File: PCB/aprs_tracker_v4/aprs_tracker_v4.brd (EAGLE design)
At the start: 100 x 35 mm, 43 parts, among them IC1 7805T, IC2 ATMEGA328PB-AUR, IC3 74LVCH1T45GW,125, IC4 REG1117, T1 2N2222, X1 BU-SMA-V, Y1 ATS080B-E

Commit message: completed aprs v4
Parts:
- removed C3: 4.7u, rcl:C050-024X044
- removed JP2: (no value), pinhead:2X03/90
- removed LED1, LED2, LED3, LED4, LED5: (no value), led:CHIP-LED0805
- added D1, D2, D3, D4, D5: (no value), led:CHIP-LED0805
- added JP4: (no value), pinhead:2X03/90
- added JP5: (no value), pinhead:2X04
- C4: device rcl:C1206 -> rcl:C0805
- C5, C7, C8, C9: device rcl:E5-6 -> rcl:C0805
- C6: device rcl:C050-024X044 -> rcl:C0805
- JP1: device pinhead:2X02 -> pinhead:2X03/90
- R1, R10, R11, R3, R5, R7, R8: device rcl:0207/7 -> rcl:R0805
- R4: device rcl:0204/7 -> rcl:R0805
- moved C9 151.0 mm to (54.2, 22.4)
- moved C8 142.3 mm to (49.2, 22.4), turned to 180 degrees
- moved R15 131.5 mm to (65.3, 7.75), turned to 180 degrees
- moved IC4 131.4 mm to (52.6, 16.0), turned to 180 degrees
- moved R6 120.4 mm to (18.8, 32.3), turned to 270 degrees
- moved S1 110.9 mm to (24.9, 30.5)
- moved C5 109.7 mm to (96.3, 9.21), turned to 90 degrees
- moved C7 103.6 mm to (96.3, 15.4), turned to 90 degrees
- moved C2 98.5 mm to (20.1, 22.9), turned to 90 degrees
- moved IC3 94.7 mm to (66.0, 10.4), turned to 90 degrees
- moved C1 87.2 mm to (20.1, 15.2), turned to 90 degrees
- moved IC1 84.0 mm to (81.7, 13.0), turned to 90 degrees
- moved Y1 79.5 mm to (15.2, 16.0), turned to 90 degrees
- moved R2 55.6 mm to (30.4, 3.30), turned to 180 degrees
- moved IC2 53.3 mm to (27.7, 18.8), flipped to the bottom
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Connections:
- new net A63: D2.A, U1.P$5
- net +3V3: now also C9.1; no longer C9.+
- net A6: no longer LED2.A, U1.P$5
- net GND: now also C5.2, C7.2, C8.2, C9.2, JP1.5, JP4.5, JP4.6, JP5.1; no longer C5.-, C7.-, C8.-, C9.-, JP1.1, JP1.3, JP2.1
- net N$10: no longer C3.2
- net N$11: no longer C3.1, R9.1
- net N$20: now also D3.C; no longer LED1.C
- net N$21: now also D2.C; no longer LED2.C
- net N$22: now also D4.C; no longer LED3.C
- net N$23: now also D3.A; no longer LED1.A
- net N$3: now also D1.C; no longer LED4.C
- net N$5: now also D5.C; no longer LED5.C
- net PIN11: now also JP4.3, JP5.3; no longer JP1.4, JP2.3
- net PIN12: now also JP4.4, JP5.6; no longer JP1.2, JP2.6
- net PIN9: now also JP1.4
- net RADIO_SQL: now also D4.A; no longer LED3.A
- net RESET: now also JP5.2; no longer JP2.2
- net RX: now also JP5.7
- net SCK: now also JP5.4; no longer JP2.4
- net SCL: now also JP1.1
- net SDA: now also JP1.2
- net TX: now also JP5.8
- net VCC: now also C7.1, C8.1, D1.A, D5.A, JP1.6, JP5.5; no longer C7.+, C8.+, JP2.5, LED4.A, LED5.A
- net V_BAT: now also C5.1, JP1.3; no longer C5.+
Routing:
- net VCC: track 0.00 -> 187.9 mm, vias 0 -> 3
- net V_BAT: track 0.00 -> 121.9 mm
- net +3V3: track 0.00 -> 97.6 mm, vias 0 -> 2
- net RADIO_WAKE: track 0.00 -> 81.0 mm, vias 0 -> 4
- net RADIO_OUTPUT_POWER: track 0.00 -> 77.7 mm, vias 0 -> 2
- net MU_TX_1: track 0.00 -> 67.9 mm
- net TO_DTMF: track 0.00 -> 65.1 mm
- net GPS_RX: track 0.00 -> 64.2 mm, vias 0 -> 1
- net N$12: track 0.00 -> 56.8 mm
- net GPS_TX: track 0.00 -> 53.1 mm, vias 0 -> 3
- net SCL: track 0.00 -> 48.9 mm
- net TX: track 0.00 -> 43.4 mm, vias 0 -> 1
- net SDA: track 0.00 -> 40.7 mm, vias 0 -> 1
- net RX: track 0.00 -> 39.0 mm, vias 0 -> 1
- net MU_RX_1: track 0.00 -> 38.5 mm, vias 0 -> 2
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- added copper zone on layer 1, net GND
- added copper zone on layer 16, net GND
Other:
- board size 100 x 35 mm -> 100.1 x 34.9 mm
- board text added: "/home/hasith/Pictures/NEBP/open_hw3.bmp"
- board text added: "3.3V"
- board text added: "APRS tracker v4.0"
- board text added: "Audio"
- board text added: "GND"
- board text added: "KE8TJE"
- board text added: "RESET"
- board text added: "RX"
- board text added: "SCL"
- board text added: "SDA"
- board text added: "TX"
- board text added: "VCC"
- board text added: "V_Bat"

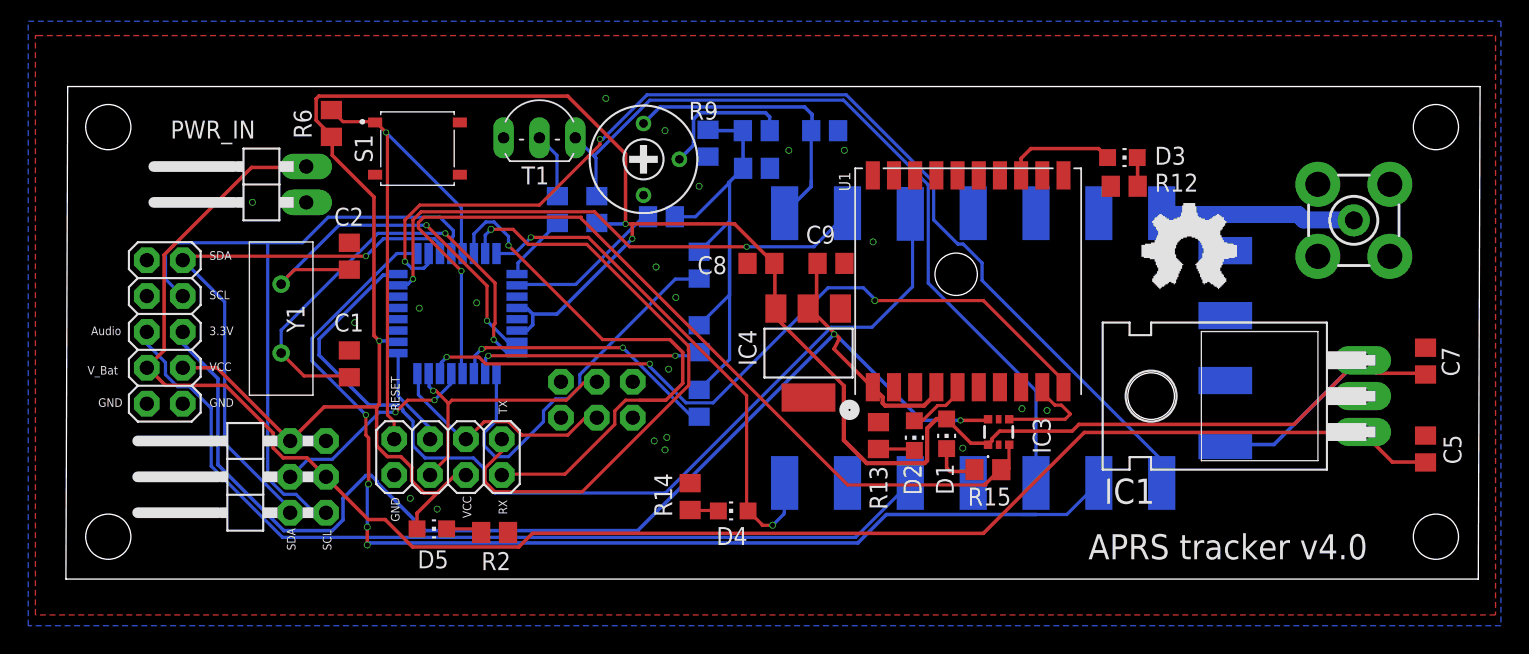
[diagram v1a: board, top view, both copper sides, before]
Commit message: fix 3v regulator location
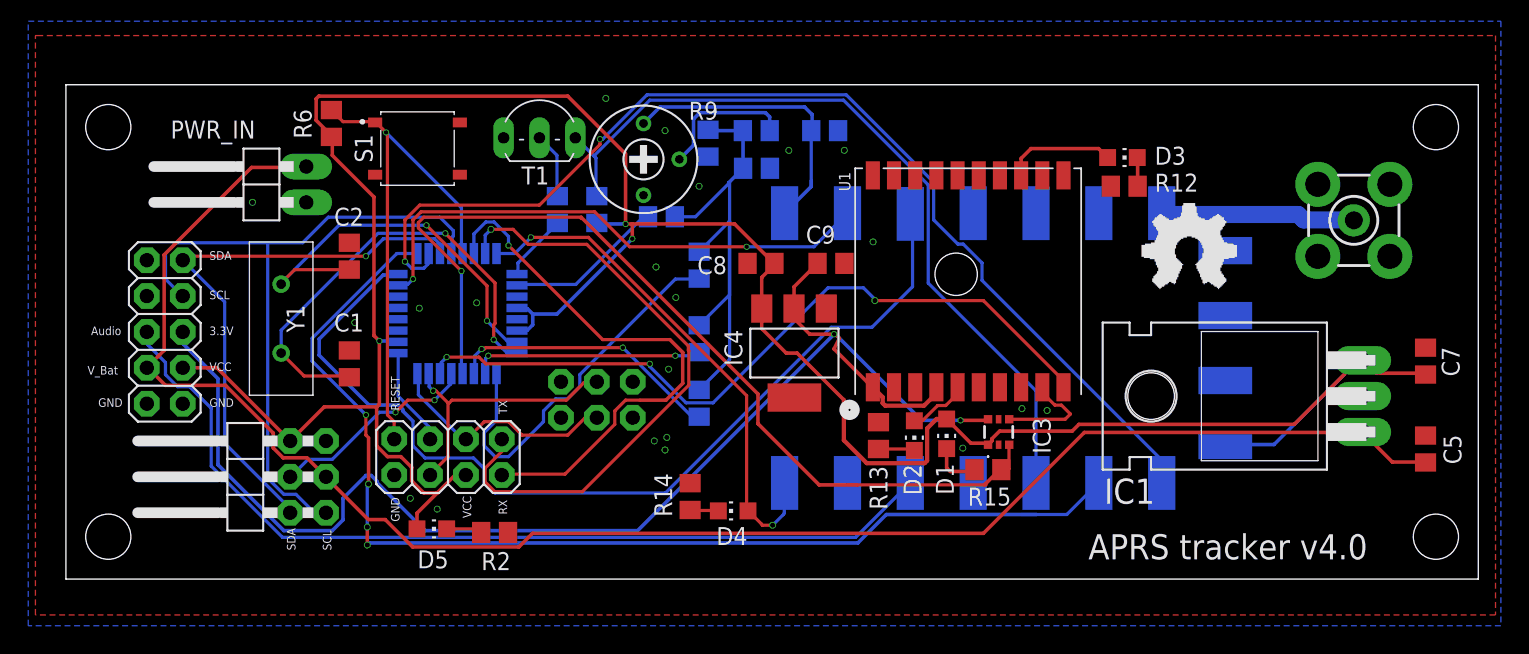
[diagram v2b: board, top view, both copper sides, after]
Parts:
- moved IC4 1.00 mm to (51.6, 16.0)
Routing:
- net +3V3: track 97.6 -> 100.2 mm
- net GPS_RX: track 64.2 -> 66.1 mm
- net VCC: track 187.9 -> 189.1 mm
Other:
- board size 100.1 x 34.9 mm -> 100 x 35 mm
- board text removed: "/home/hasith/Pictures/NEBP/open_hw3.bmp"
